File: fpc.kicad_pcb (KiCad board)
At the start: 2 copper layers, 251.1 x 145.4 mm, 91 parts, among them J16 Screw_Terminal_01x04, J17 Screw_Terminal_01x04, J18 Screw_Terminal_01x04, J19 Screw_Terminal_01x04, J20 Screw_Terminal_01x04, J21 Screw_Terminal_01x04, J22 15v, J3 Screw_Terminal_01x04, J4 Screw_Terminal_01x04, J5 Conn_01x02_Socket, J6 Conn_01x16_Socket, J7 Conn_01x16_Socket, K1 Relay_SPDT, K2 Relay_SPDT, K3 Relay_SPDT, K4 Relay_SPDT, Q1 BC547, Q6 BC547, Q7 BC547, Q8 BC547, U5 DEVKIT_V1_ESP32-WROOM-32, U6 RS485_TTL_Module, U7 ZC261500

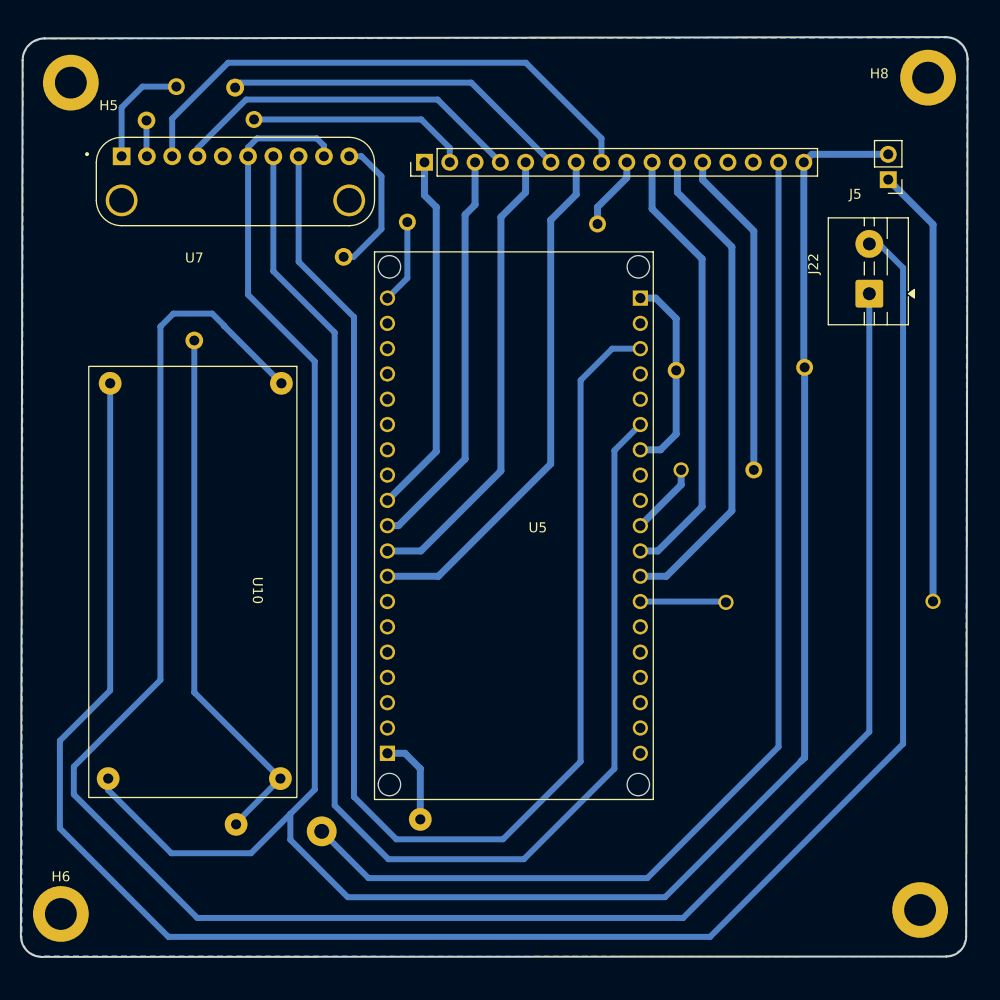
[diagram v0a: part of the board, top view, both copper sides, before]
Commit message: - Changing of PCB Layout - Change the microcontroller from ESP32 to ESP32 S3 - Reroute the board
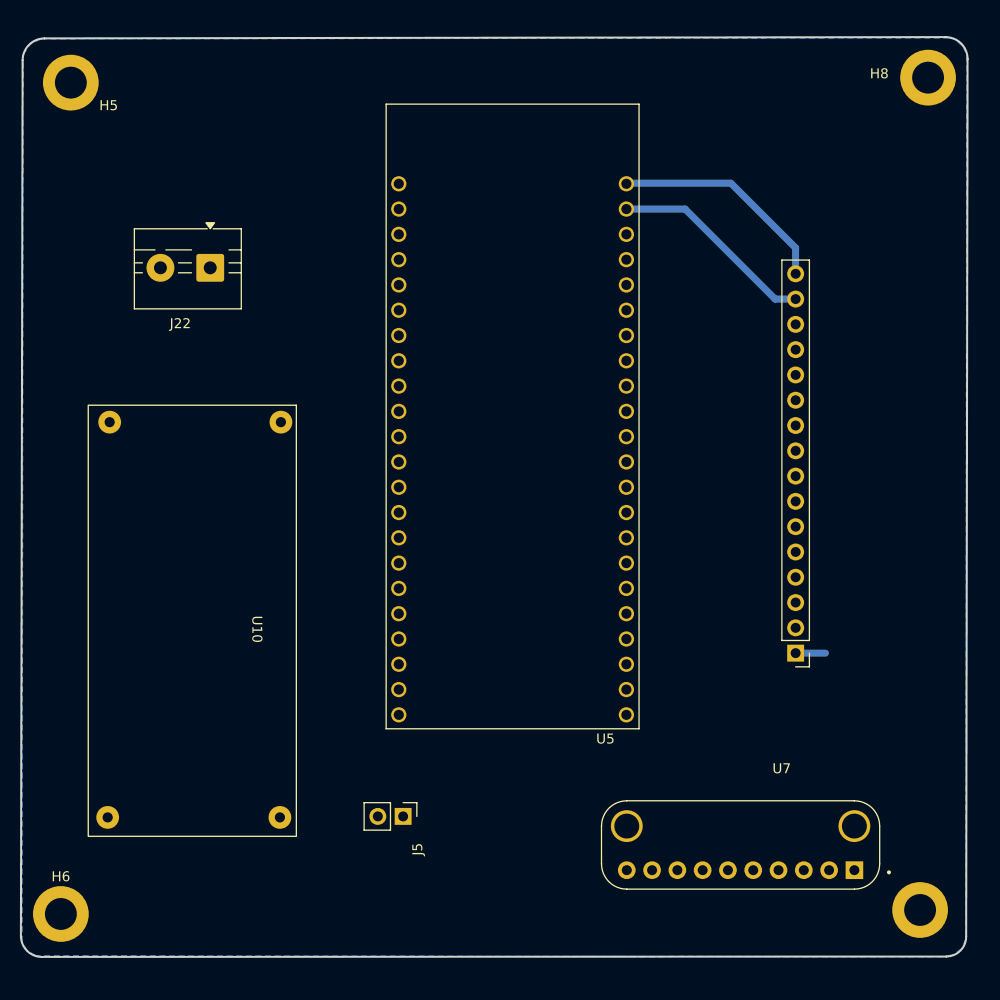
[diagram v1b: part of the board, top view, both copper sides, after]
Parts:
- removed the ? at (154.6, 137.2)
- removed the ? at (109.9, 172.8)
- removed the ? at (105.7, 124.2)
- removed the ? at (118.5, 173.5)
- removed the ? at (103.9, 98.7)
- removed the ? at (159.1, 150.5)
- removed the ? at (127.1, 112.3)
- removed the ? at (128.4, 172.3)
- removed the ? at (120.7, 115.8)
- removed the ? at (109.8, 98.8)
- removed the ? at (161.9, 137.2)
- removed the ? at (167.0, 126.9)
- removed the ? at (154.1, 127.2)
- removed the ? at (100.9, 102.1)
- removed the ? at (146.2, 112.5)
- removed the ? at (111.7, 102.0)
- removed the ? at (179.9, 150.4)
- U5: value DEVKIT_V1_ESP32-WROOM-32 -> ESP32-S3-DEVKITC-1U-N8R8; footprint custom:MODULE_ESP32_NODEMCU -> RF_Module:MODULE_ESP32-S3-DEVKITC-1U-N8R8
- moved J5 80.4 mm to (126.7, 172.0), turned to -90 degrees
- moved U7 77.3 mm to (160.6, 170.7), turned to 0 degrees
- moved J22 66.3 mm to (107.3, 116.9), turned to 180 degrees
- moved J6 61.8 mm to (166.1, 155.6), turned to 180 degrees
- moved U5 11.0 mm to (137.7, 131.8), turned to 180 degrees
- moved U10 3.90 mm to (106.2, 153.2)
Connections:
- net /R1 renamed /RELAY_1
- net /R2 renamed /RELAY_2
- net /R3 renamed /RELAY_3
- net /R4 renamed /RELAY_4
- J6 pad 1: /GPIO25 -> /GPIO14
- J6 pad 10: /D1+ -> /RX_PIN
- J6 pad 11: /R0+ -> /DRI
- J6 pad 12: /RE+ -> /TX_PIN
- J6 pad 3: /GPIO26 -> /GPIO17
- J6 pad 5: /GPIO27 -> /GPIO18
- J6 pad 7: /GPIO14 -> /GPIO21
- J7 pad 10: /D1 -> /RX_PIN
- J7 pad 11: /R0 -> /DRI
- J7 pad 12: /RE -> /TX_PIN
- K4 pad 1: /2AC+ -> unconnected-(K4-Pad1)
- U6 pad 1: /R0 -> /RX_PIN
- U6 pad 2: /RE -> /DRI
- U6 pad 3: /RE -> /DRI
- U6 pad 4: /D1 -> /TX_PIN
- U7 pad 7: Net-(U5-IO21) -> /SDA
- U7 pad 8: Net-(U5-IO22) -> /SCL
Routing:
- net GND: track 436.2 -> 203.3 mm
- net Net-(J22-Pin_1): track 203.0 -> 0.00 mm
- net Net-(J22-Pin_2): track 196.2 -> 0.00 mm
- net +5V: track 189.2 -> 20.7 mm
- net (no net): track 0.00 -> 146.8 mm
- net Net-(U5-IO22): track 140.0 -> 0.00 mm
- net Net-(U5-IO21): track 137.5 -> 0.00 mm
- net /R0: track 79.8 -> 0.00 mm
- net /D1: track 67.0 -> 0.00 mm
- net /A1+: track 54.8 -> 0.00 mm
- net /GPIO4: track 52.9 -> 0.00 mm
- net /GPIO14: track 52.4 -> 3.00 mm
- net /R0+: track 49.2 -> 0.00 mm
- net /GPIO27: track 46.8 -> 0.00 mm
- net /A3+: track 46.5 -> 0.00 mm
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
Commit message: - Change the Microcontroller from esp32 to esp32 s3 - Add the updated PCB design/rerouting
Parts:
- added ?: , , F.Cu at (133.4, 155.7)
- added ?: , , F.Cu at (166.0, 160.8)
- added ?: , , F.Cu at (145.9, 155.7)
- added ?: , , F.Cu at (153.2, 144.1)
- added ?: , , F.Cu at (170.3, 140.6)
- added ?: , , F.Cu at (155.8, 121.2)
- added ?: , , F.Cu at (155.7, 131.2)
- added ?: , , F.Cu at (170.1, 120.1)
- added ?: , , F.Cu at (170.4, 135.0)
- added ?: , , F.Cu at (142.8, 170.4)
- added ?: , , F.Cu at (162.7, 152.0)
- added ?: , , F.Cu at (158.0, 135.4)
- added ?: , , F.Cu at (156.2, 146.6)
- added ?: , , F.Cu at (177.6, 119.7)
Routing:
- net +5V: track 20.7 -> 247.9 mm
- net GND: track 203.3 -> 312.8 mm
- net /GPIO21: track 0.00 -> 94.8 mm
- net /GPIO14: track 3.00 -> 72.6 mm
- net /A1+: track 0.00 -> 59.5 mm
- net /SCL: track 0.00 -> 46.8 mm
- net /A3+: track 0.00 -> 42.6 mm
- net /SDA: track 0.00 -> 41.5 mm
- net /A0+: track 0.00 -> 35.4 mm
- net /A2+: track 0.00 -> 30.8 mm
- net 3.3V: track 0.00 -> 28.8 mm
- net /GPIO4: track 0.00 -> 25.8 mm
- net /GPIO18: track 0.00 -> 20.7 mm
- net /TX_PIN: track 0.00 -> 18.6 mm
- net /DRI: track 2.54 -> 21.2 mm
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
